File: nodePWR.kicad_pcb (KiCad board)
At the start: 2 copper layers, 34 x 20.5 mm, 17 parts, among them P1 Vin (4.5-30VDC), P2 USB (power only), P3 Node, P4 Serial I/O, P5 BAT, SW1 Prgm, U1 bq25070

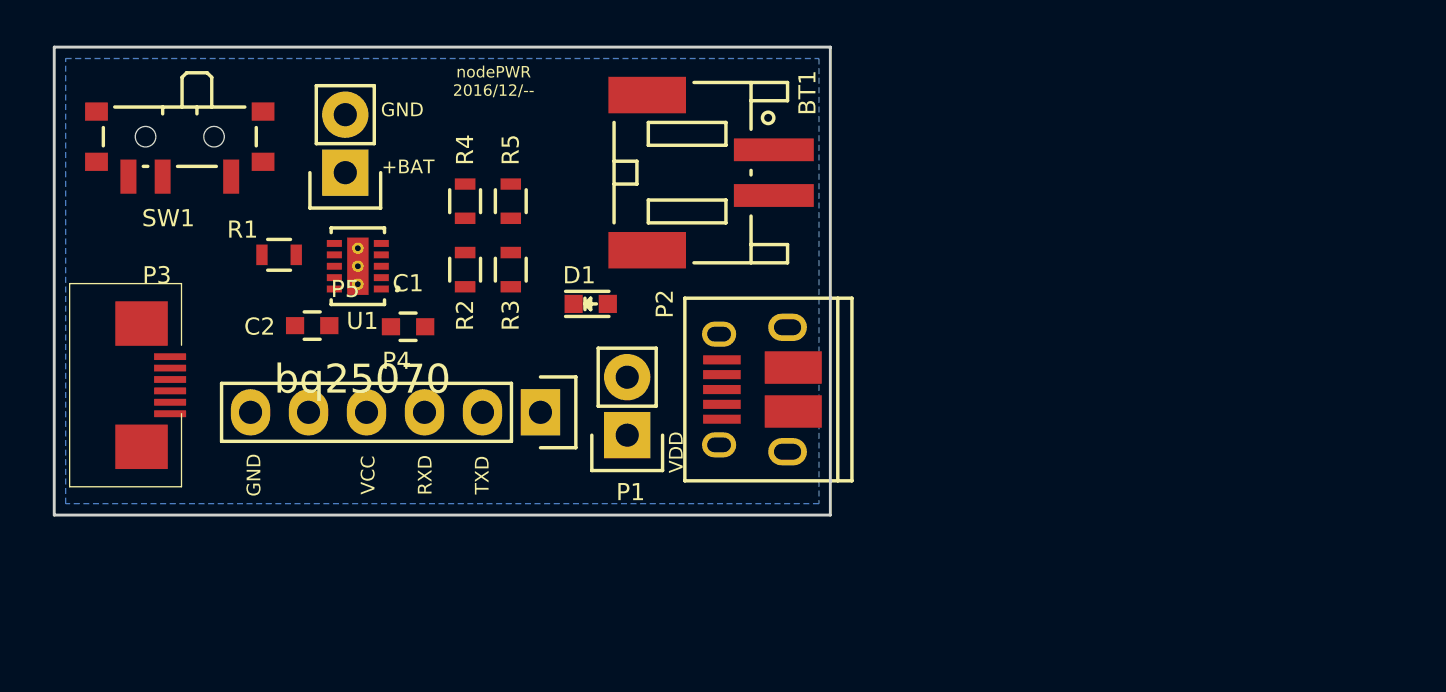
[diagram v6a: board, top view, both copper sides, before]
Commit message: Checkpoint - routed
    - passes DRC
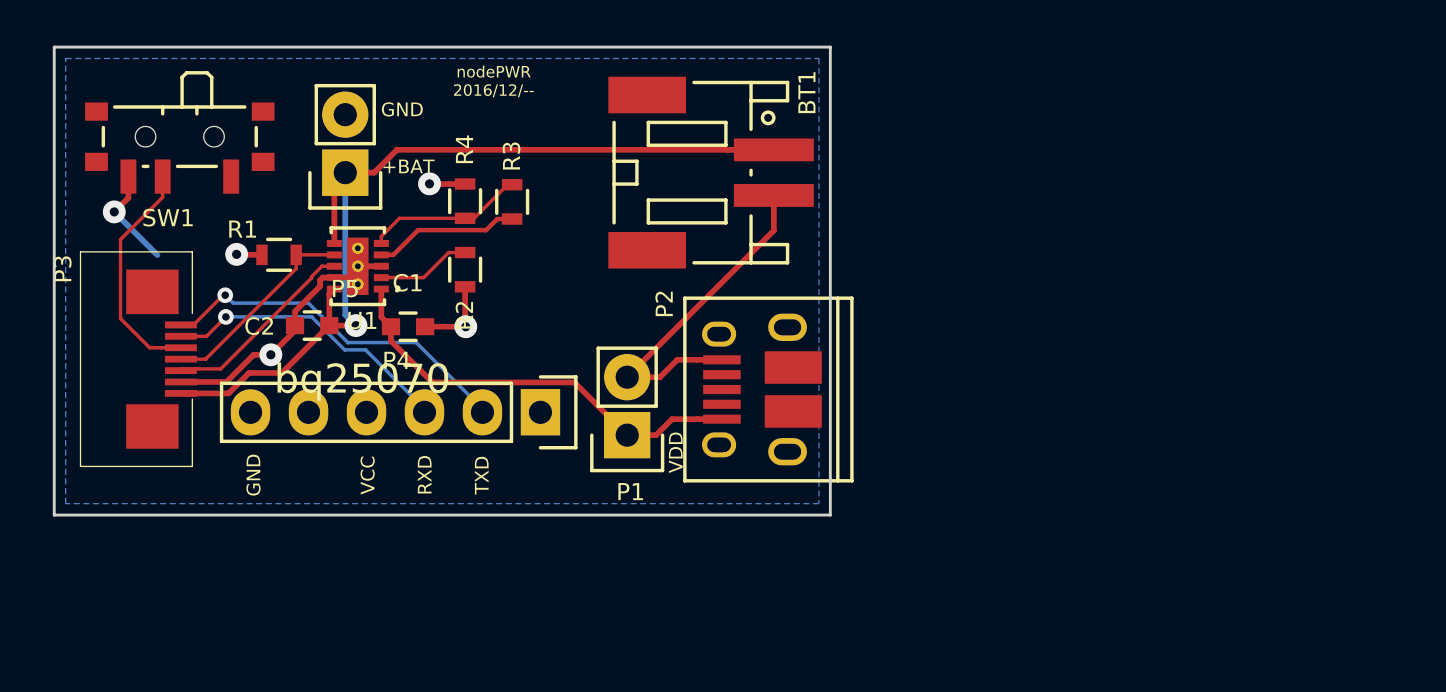
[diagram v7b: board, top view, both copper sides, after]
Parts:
- removed D1: Charging, LEDs:LED_0603
- removed R5: 100k, Resistors_SMD:R_0603
- removed Ref**: RockingDLogo_9x7, rockingDLogos:RockingDLogo_9x7
- P3: footprint rockingdlabs:FPC_conn-6_8x4.9mm_Pitch0.5mm -> rockingdlabs:FPC_conn-7_8x4.9mm_Pitch0.5mm
- R3: value 75 -> 487k
- R4: value 490k -> 100k
- moved R3 2.97 mm to (120.1, 106.8), turned to 90 degrees
- moved P3 1.23 mm to (103.8, 113.7)
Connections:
- P3 pad 3: /VCC -> /PGM
- P3 pad 4: /PGM -> /CTRL
- P3 pad 5: GND -> /CHRG
- P3 pad 6: +BATT -> GND
- P4 pad 4: /VCC -> Net-(P4-Pad4)
- R1 pad 1: Net-(R1-Pad1) -> /CTRL
- R3 pad 2: Net-(D1-Pad2) -> Net-(R3-Pad2)
- R4 pad 1: +3V3 -> Net-(R3-Pad2)
- R4 pad 2: Net-(R4-Pad2) -> GND
- U1 pad 5: Net-(R4-Pad2) -> Net-(R3-Pad2)
- U1 pad 7: Net-(R1-Pad1) -> /CTRL
- U1 pad 8: Net-(D1-Pad1) -> /CHRG
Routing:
- net +BATT: track 0.00 -> 40.0 mm, vias 0 -> 1
- net GND: track 0.00 -> 37.4 mm, vias 0 -> 5
- net VDD: track 0.00 -> 18.9 mm
- net /TXD: track 0.00 -> 16.0 mm, vias 0 -> 1
- net /RXD: track 0.00 -> 12.8 mm, vias 0 -> 1
- net /PGM: track 0.00 -> 10.2 mm
- net /CTRL: track 0.00 -> 8.97 mm
- net /CHRG: track 0.00 -> 8.65 mm
- net Net-(R3-Pad2): track 0.00 -> 6.98 mm
- net +3V3: track 0.00 -> 6.38 mm
- net Net-(R2-Pad1): track 0.00 -> 4.13 mm
